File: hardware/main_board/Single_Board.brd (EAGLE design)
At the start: 49.9 x 49.6 mm, 38 parts, among them J1 5520425-3, J2 U.FL, J3 AVR_SPI_PROG_3X2NS, Q1 200mA/40V, Q2 220mA/50V/3.5Ω, U2 MCP1703T-3302E/CB, U3 W25X40CLSNIG, U5 ATMEGA328PB-AU, X2 B2B-PH-K-S, X3 B2B-XH-2, Y1 8MHz

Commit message: More PCB work
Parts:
- moved C8 9.30 mm to (22.4, 13.4)
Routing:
- net VCC: track 156.2 -> 153.4 mm
- net SCK: track 63.2 -> 61.9 mm
- net MOSI: track 73.8 -> 73.2 mm
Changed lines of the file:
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@@
 <attribute name="VALUE" x="41.032" y="7.73" size="0.6096" layer="27" font="vector" ratio="20" rot="R90"/>
 </element>
-<element name="C8" library="SparkFun-Capacitors" library_urn="urn:adsk.eagle:library:510" package="0805" package3d_urn="urn:adsk.eagle:package:37429/1" value="1.0uF" x="25.4" y="4.6" smashed="yes" rot="MR270">
-<attribute name="NAME" x="24.511" y="4.6" size="0.6096" layer="26" font="vector" ratio="20" rot="MR270" align="bottom-center"/>
-<attribute name="PROD_ID" value="CAP-08064" x="51.4" y="52.6" size="1.778" layer="28" rot="MR270" display="off"/>
-<attribute name="VALUE" x="26.289" y="4.6" size="0.6096" layer="28" font="vector" ratio="20" rot="MR270" align="top-center"/>
+<element name="C8" library="SparkFun-Capacitors" library_urn="urn:adsk.eagle:library:510" package="0805" package3d_urn="urn:adsk.eagle:package:37429/1" value="1.0uF" x="22.4" y="13.4" smashed="yes" rot="MR270">
+<attribute name="NAME" x="21.511" y="13.4" size="0.6096" layer="26" font="vector" ratio="20" rot="MR270" align="bottom-center"/>
+<attribute name="PROD_ID" value="CAP-08064" x="48.4" y="61.4" size="1.778" layer="28" rot="MR270" display="off"/>
+<attribute name="VALUE" x="23.289" y="13.4" size="0.6096" layer="28" font="vector" ratio="20" rot="MR270" align="top-center"/>
 </element>
 <element name="Y1" library="SparkFun-Clocks" library_urn="urn:adsk.eagle:library:511" package="RESONATOR-SMD-3.2X1.3" package3d_urn="urn:adsk.eagle:package:37551/1" value="8MHz" x="22" y="17.4" smashed="yes" rot="MR90">
@@
 <attribute name="MANUFACTURER_PART_NUMBER" value="W25X40CLSNIG" x="63.4" y="28" size="1.778" layer="28" rot="MR270" display="off"/>
 <attribute name="NAME" x="21.035" y="9.2766" size="1.27" layer="26" ratio="6" rot="SMR270"/>
-<attribute name="VALUE" x="21.035" y="7.7272" size="1.27" layer="22" ratio="6" rot="SMR270"/>
 <attribute name="VENDOR" value="Winbond" x="63.4" y="28" size="1.778" layer="28" rot="MR270" display="off"/>
 </element>
@@
 <wire x1="34.27" y1="26.96" x2="34.27" y2="24.47" width="0.1524" layer="1"/>
 <wire x1="34.27" y1="24.47" x2="34.26" y2="24.46" width="0.1524" layer="1"/>
-<wire x1="34.27" y1="26.96" x2="34.04" y2="26.96" width="0.1524" layer="1"/>
 <wire x1="36.29" y1="26.56" x2="34.27" y2="27.42" width="0.1524" layer="1"/>
 <wire x1="34.27" y1="27.42" x2="34.27" y2="26.96" width="0.1524" layer="1"/>
@@
 <wire x1="21.035" y1="6.6" x2="21.035" y2="8.4638" width="0.1524" layer="16"/>
 <wire x1="19.765" y1="4.965" x2="21.035" y2="6.235" width="0.1524" layer="16"/>
-<wire x1="25.4" y1="5.5" x2="24.5" y2="5.5" width="0.1524" layer="16"/>
-<wire x1="23.4" y1="6.6" x2="21.035" y2="6.6" width="0.1524" layer="16"/>
-<wire x1="24.5" y1="5.5" x2="23.4" y2="6.6" width="0.1524" layer="16"/>
-<wire x1="21.035" y1="6.6" x2="16.2" y2="6.6" width="0.1524" layer="16"/>
+<wire x1="16.2" y1="6.6" x2="21.035" y2="6.6" width="0.1524" layer="16"/>
 <wire x1="16.2" y1="6.6" x2="13.6" y2="9.2" width="0.1524" layer="16"/>
 <wire x1="13.6" y1="9.2" x2="13.6" y2="11.2" width="0.1524" layer="16"/>
@@
 <wire x1="32.2" y1="16" x2="30.8" y2="14.6" width="0.1524" layer="16"/>
 <wire x1="30.8" y1="14.6" x2="26.2" y2="14.6" width="0.1524" layer="16"/>
-<wire x1="16" y1="11.3" x2="17.3" y2="10" width="0.1524" layer="16"/>
-<wire x1="17.3" y1="10" x2="17.4" y2="10" width="0.1524" layer="16"/>
-<via x="17.4" y="10" extent="1-16" drill="0.35"/>
-<wire x1="17.4" y1="10" x2="19.4" y2="10" width="0.1524" layer="1"/>
-<wire x1="19.4" y1="10" x2="23" y2="13.6" width="0.1524" layer="1"/>
-<via x="23" y="13.6" extent="1-16" drill="0.35"/>
-<wire x1="23" y1="13.6" x2="24.82" y2="13.6" width="0.1524" layer="16"/>
+<via x="23.4" y="8.2" extent="1-16" drill="0.35"/>
+<wire x1="23.4" y1="8.2" x2="23.4" y2="9.8" width="0.1524" layer="1"/>
+<wire x1="23.4" y1="9.8" x2="26.6" y2="13" width="0.1524" layer="1"/>
+<via x="26.6" y="13" extent="1-16" drill="0.35"/>
+<wire x1="26.2" y1="13.6" x2="26.2" y2="13.4" width="0.1524" layer="16"/>
+<wire x1="26.2" y1="13.4" x2="26.6" y2="13" width="0.1524" layer="16"/>
+<wire x1="22.4" y1="14.3" x2="23.1" y2="13.6" width="0.1524" layer="16"/>
+<wire x1="23.1" y1="13.6" x2="24.82" y2="13.6" width="0.1524" layer="16"/>
+<wire x1="21.035" y1="6.6" x2="22.6" y2="6.6" width="0.1524" layer="16"/>
+<wire x1="23.4" y1="7.4" x2="23.4" y2="8.2" width="0.1524" layer="16"/>
+<wire x1="22.6" y1="6.6" x2="23.4" y2="7.4" width="0.1524" layer="16"/>
 </signal>
 <signal name="GND">
@@
 </polygon>
 <via x="31.6" y="22.2" extent="1-16" drill="0.35"/>
-<via x="21.8" y="14.4" extent="1-16" drill="0.35"/>
+<via x="20.8" y="12.8" extent="1-16" drill="0.35"/>
 </signal>
 <signal name="SDA">
@@
 <wire x1="31.595" y1="25.325" x2="28.2" y2="25.325" width="0.1524" layer="1"/>
 <contactref element="U5" pad="27"/>
-<wire x1="30.2" y1="9.82" x2="30.4" y2="10.02" width="0.1524" layer="16"/>
 <via x="30.4" y="12.4" extent="1-16" drill="0.35"/>
 <wire x1="30.4" y1="12.4" x2="30.2" y2="12.6" width="0.1524" layer="1"/>
@@
 <contactref element="R6" pad="2"/>
 <wire x1="26.2" y1="9.82" x2="26.18" y2="9.8" width="0.1524" layer="16"/>
-<wire x1="22.2" y1="11.6" x2="20" y2="11.6" width="0.1524" layer="16"/>
+<wire x1="22.2" y1="11.4" x2="20.2" y2="11.4" width="0.1524" layer="16"/>
+<wire x1="20.2" y1="11.4" x2="20" y2="11.6" width="0.1524" layer="16"/>
 <via x="20" y="11.6" extent="1-16" drill="0.35"/>
 <wire x1="20" y1="11.6" x2="18" y2="11.6" width="0.1524" layer="1"/>
@@
 <wire x1="13.8" y1="12.8" x2="13.35" y2="13.25" width="0.1524" layer="16"/>
 <wire x1="13.35" y1="13.25" x2="13.35" y2="14.2" width="0.1524" layer="16"/>
-<wire x1="26.18" y1="9.8" x2="24" y2="9.8" width="0.1524" layer="16"/>
-<wire x1="24" y1="9.8" x2="22.2" y2="11.6" width="0.1524" layer="16"/>
+<wire x1="26.18" y1="9.8" x2="23.8" y2="9.8" width="0.1524" layer="16"/>
+<wire x1="23.8" y1="9.8" x2="22.2" y2="11.4" width="0.1524" layer="16"/>
 <wire x1="12.3" y1="11.4" x2="13.7" y2="12.8" width="0.1524" layer="16"/>
 <wire x1="13.7" y1="12.8" x2="13.8" y2="12.8" width="0.1524" layer="16"/>
@@
 <wire x1="21.422225" y1="22" x2="20.840825" y2="22.5814" width="0.1524" layer="1"/>
 <wire x1="16.2" y1="16.2" x2="16.2" y2="3.6" width="0.1524" layer="1"/>
-<wire x1="22.305" y1="1.6" x2="22.305" y2="3.5362" width="0.1524" layer="16"/>
-<wire x1="16.2" y1="3.6" x2="18.2" y2="1.6" width="0.1524" layer="16"/>
-<wire x1="18.2" y1="1.6" x2="22.305" y2="1.6" width="0.1524" layer="16"/>
+<wire x1="22.305" y1="2" x2="22.305" y2="3.5362" width="0.1524" layer="16"/>
+<wire x1="16.2" y1="3.6" x2="17.8" y2="2" width="0.1524" layer="16"/>
+<wire x1="17.8" y1="2" x2="22.305" y2="2" width="0.1524" layer="16"/>
 <wire x1="42.73" y1="23" x2="38.73" y2="27" width="0.1524" layer="16"/>
 <wire x1="38.73" y1="27" x2="22.8" y2="27" width="0.1524" layer="16"/>
@@
 <contactref element="U5" pad="17"/>
 <contactref element="J3" pad="3"/>
-<wire x1="20.5" y1="23.1" x2="20.5" y2="24.4" width="0.1524" layer="16"/>
 <via x="20.6" y="22" extent="1-16" drill="0.35"/>
 <wire x1="20.6" y1="22" x2="20.5" y2="22.1" width="0.1524" layer="16"/>
@@
 <wire x1="25.4" y1="46" x2="25.375" y2="46" width="0.1524" layer="1"/>
 <wire x1="20.5" y1="41.5" x2="21.8" y2="42.8" width="0.1524" layer="16"/>
-<wire x1="22.625" y1="46" x2="22.625" y2="48.625" width="0.1524" layer="1"/>
-<wire x1="22.625" y1="48.625" x2="23" y2="49" width="0.1524" layer="1"/>
-<wire x1="23" y1="49" x2="25.2" y2="49" width="0.1524" layer="1"/>
-<wire x1="25.2" y1="49" x2="25.6" y2="48.6" width="0.1524" layer="1"/>
+<wire x1="22.625" y1="46" x2="22.625" y2="48.6" width="0.1524" layer="1"/>
+<wire x1="22.625" y1="48.6" x2="25.6" y2="48.6" width="0.1524" layer="1"/>
 <wire x1="25.6" y1="48.6" x2="25.6" y2="46.2" width="0.1524" layer="1"/>
 <wire x1="25.6" y1="46.2" x2="25.4" y2="46" width="0.1524" layer="1"/>
@@
 <contactref element="U5" pad="20"/>
 <contactref element="C3" pad="2"/>
-<wire x1="33.18" y1="14.4" x2="33.33" y2="14.55" width="0.1524" layer="16"/>
 <wire x1="36.15" y1="14.4" x2="36.6" y2="14.85" width="0.1524" layer="16"/>
 <wire x1="33.18" y1="14.4" x2="36.15" y2="14.4" width="0.1524" layer="16"/>

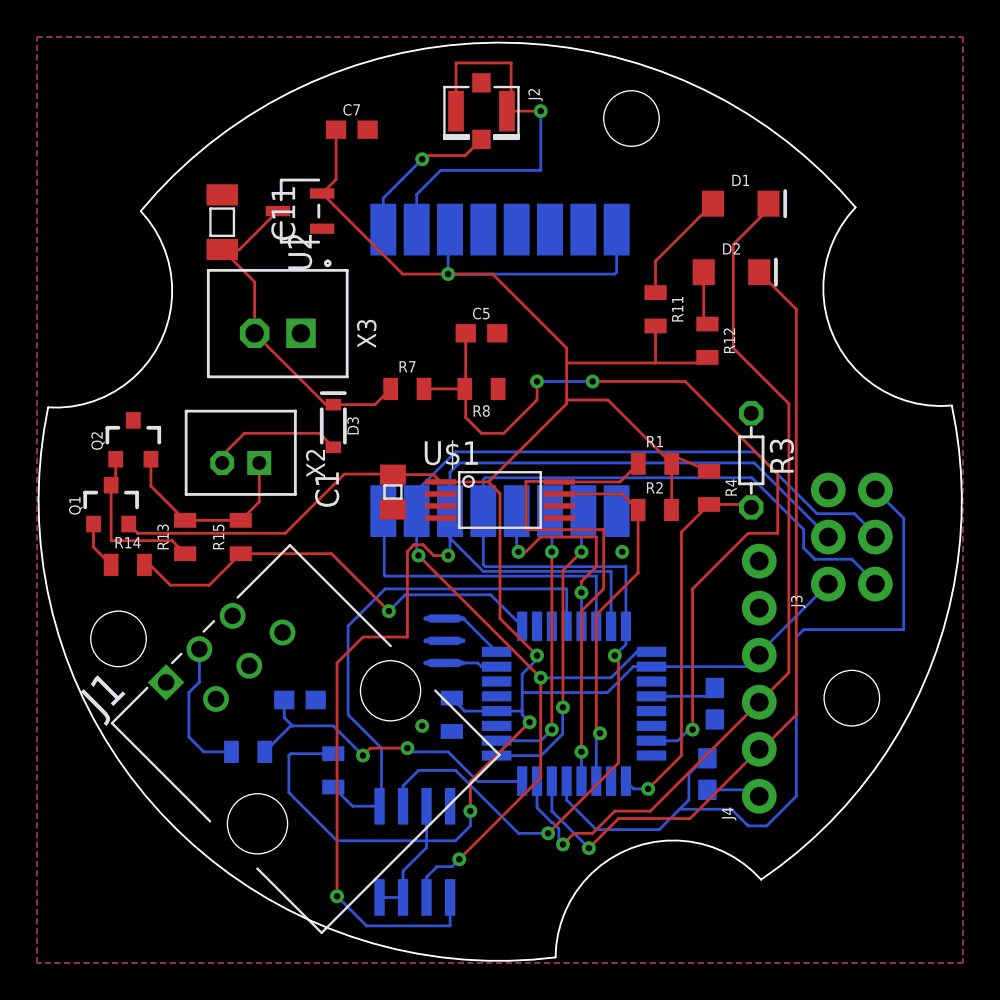
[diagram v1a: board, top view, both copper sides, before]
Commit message: Hardware work. Added elevation to station meta data
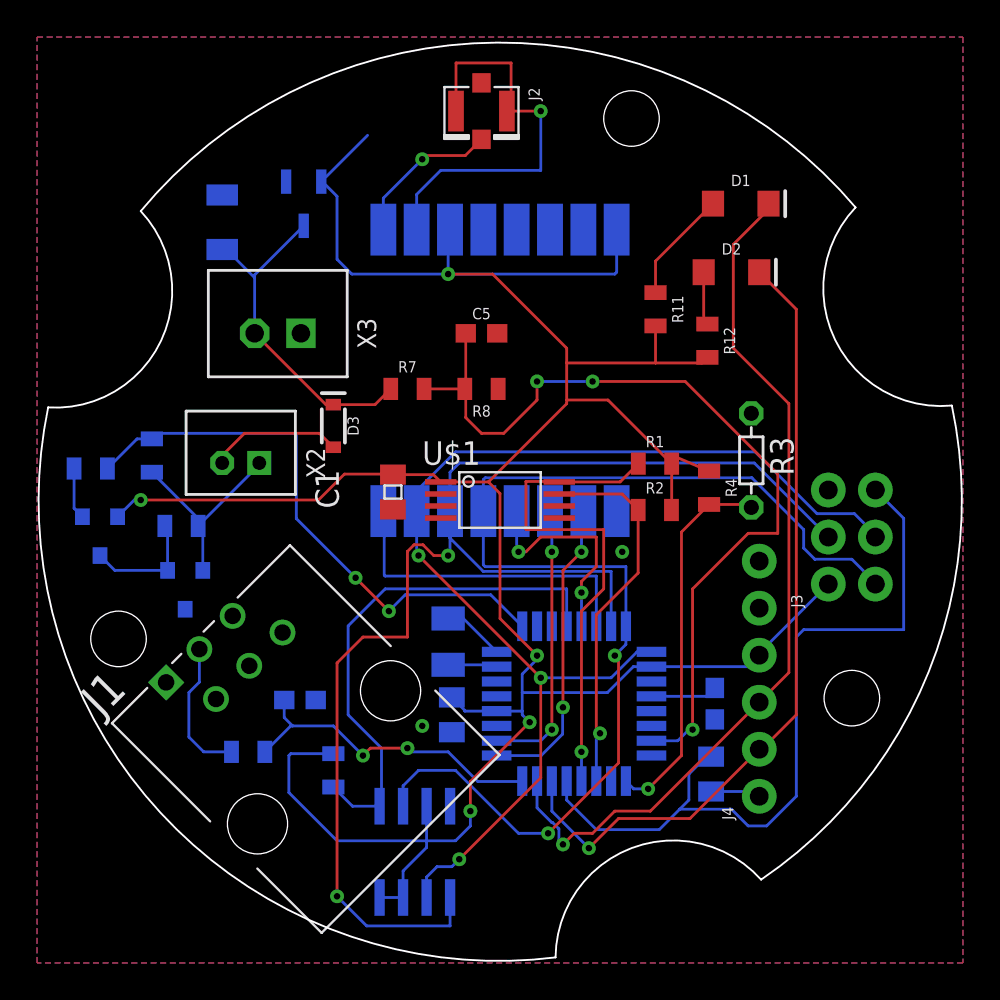
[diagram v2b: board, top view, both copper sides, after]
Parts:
- removed C7: 1.0uF, SparkFun-Capacitors:0603
- removed C8: 1.0uF, SparkFun-Capacitors:0805
- removed Y1: 8MHz, SparkFun-Clocks:RESONATOR-SMD-3.2X1.3
- added C6: 1uF, capsmd:0805
- added X1: 32.768KHZ-FC-135, main_board:32.768KHZ-FC-135
- C4: device SparkFun-Capacitors:0603 -> main_board:0805
- R11, R12: value (none) -> 1k
- moved Q2 8.48 mm to (8.00, 20.2), flipped to the bottom, turned to 180 degrees
- moved R15 6.51 mm to (6.20, 27.4), flipped to the bottom, turned to 270 degrees
- moved R14 5.57 mm to (2.90, 26.7), flipped to the bottom, turned to 180 degrees
- moved Q1 1.71 mm to (3.40, 23.1), flipped to the bottom, turned to 180 degrees
- moved R13 0.63 mm to (7.80, 23.6), flipped to the bottom, turned to 180 degrees
- moved U2 0.45 mm to (14.4, 41.0), flipped to the bottom, turned to 180 degrees
- moved C4 0.20 mm to (36.4, 10.2), turned to 90 degrees
- flipped C11 to the bottom
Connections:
- net AT_RST: now also C4.2; no longer C4.1
- net GND: now also C6.1; no longer C7.2, C8.2, Y1.2
- net N$11: now also C4.1; no longer C4.2
- net N$7: now also X1.2; no longer Y1.1
- net N$8: now also X1.1; no longer Y1.3
- net VCC: now also C6.2; no longer C7.1, C8.1
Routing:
- net PWM_SOLAR: track 23.9 -> 30.9 mm, vias 1 -> 2
- net N$12: track 8.79 -> 6.44 mm
- net VCC: track 153.4 -> 155.5 mm, vias 4 -> 5
- net N$9: track 10.6 -> 11.2 mm

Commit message: Reworked board to put more components on bottom side (=less soldering)
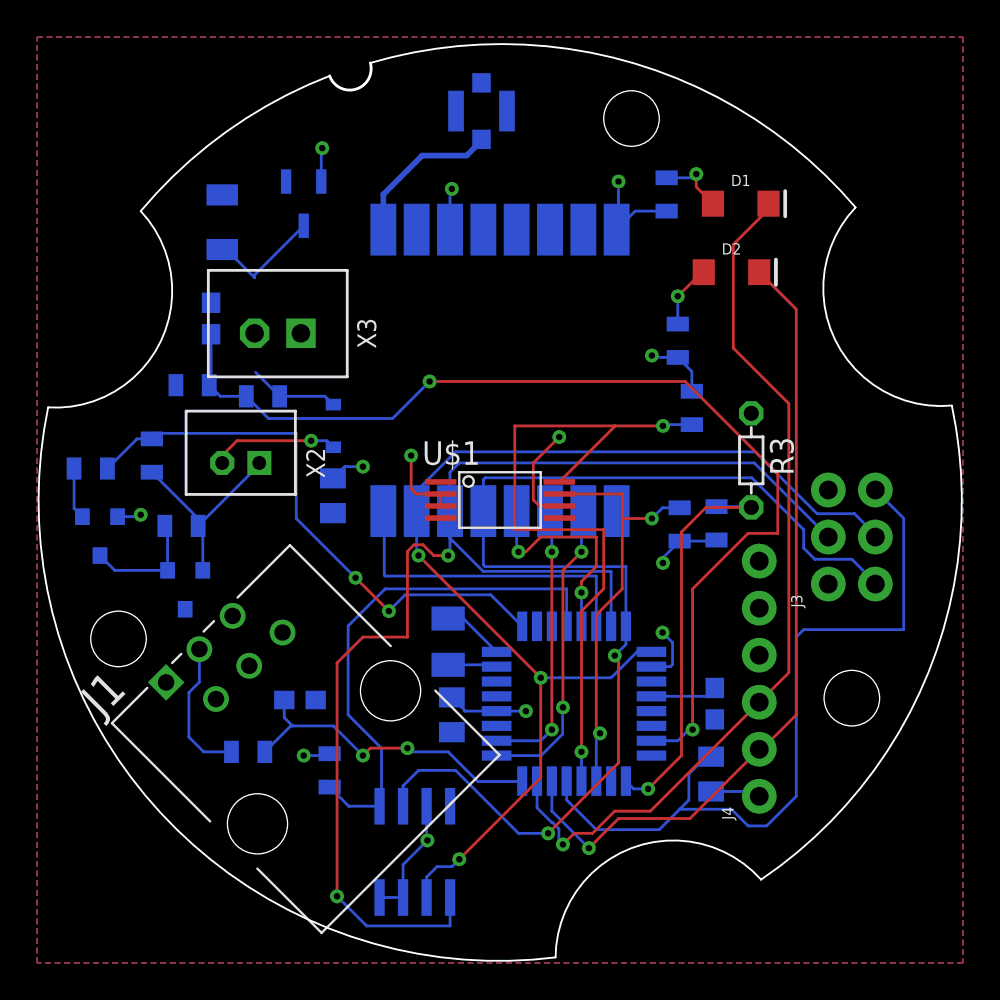
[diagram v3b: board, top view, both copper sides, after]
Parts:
- moved R8 15.6 mm to (8.40, 31.2), flipped to the bottom
- moved C5 14.6 mm to (9.40, 34.8), flipped to the bottom, turned to 90 degrees
- moved R7 7.81 mm to (12.2, 30.6), flipped to the bottom
- moved R11 6.23 mm to (34.0, 41.5), flipped to the bottom
- moved R1 3.61 mm to (35.4, 30.0), flipped to the bottom, turned to 90 degrees
- moved C1 3.25 mm to (16.0, 25.2), flipped to the bottom
- moved R4 1.96 mm to (36.7, 23.7), flipped to the bottom, turned to 90 degrees
- moved R12 1.60 mm to (34.6, 33.6), flipped to the bottom
- moved R2 1.55 mm to (34.7, 23.7), flipped to the bottom, turned to 270 degrees
- moved R9 0.20 mm to (15.8, 10.4)
- flipped D3 to the bottom
- flipped J2 to the bottom
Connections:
- removed net RF_GND: J2.1, J2.2, U$2.GND@1
- net GND: now also J2.1, J2.2, U$2.GND@1
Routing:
- net VCC: track 155.5 -> 36.4 mm, vias 5 -> 11
- net RF_GND: track 22.4 -> 0.00 mm, vias 1 -> 0
- net SCL: track 27.4 -> 38.3 mm, vias 1 -> 2
- net GND: track 0.00 -> 9.68 mm
- net BATT_SENSE: track 47.0 -> 56.3 mm, vias 3 -> 2
- net VIN: track 18.6 -> 11.3 mm
- net SDA: track 20.4 -> 23.0 mm, vias 1 -> 2
- net N$4: track 6.08 -> 3.66 mm, vias 0 -> 1
- net TEMP_SENSE: track 20.4 -> 22.2 mm
- net N$6: track 2.88 -> 3.44 mm, vias 0 -> 1
- net VSOLAR: track 7.21 -> 6.88 mm, vias 0 -> 1
- net ANT: track 8.32 -> 8.48 mm, vias 1 -> 0
- added copper zone on layer 1, net VCC
- removed copper zone on layer 1, net GND
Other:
- board size 49.9 x 49.6 mm -> 49.9 x 49.5 mm

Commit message: Added daylight indicators
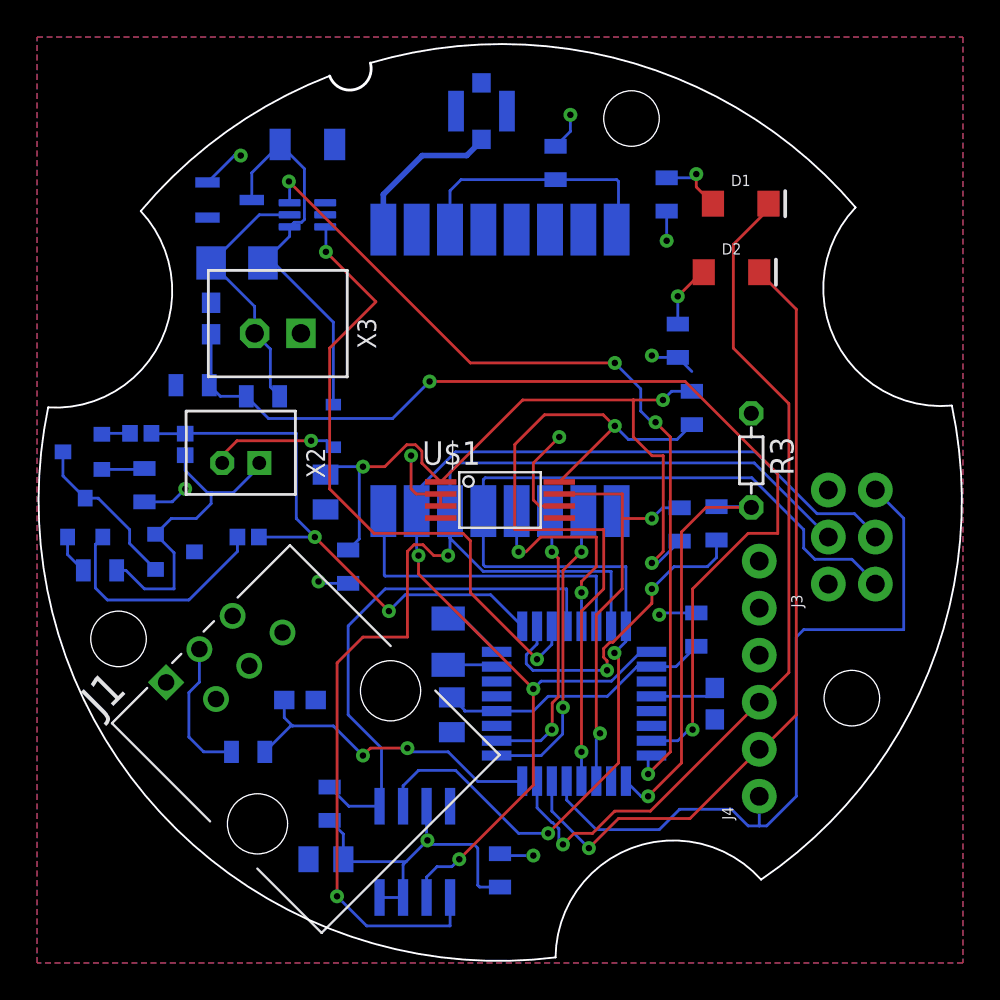
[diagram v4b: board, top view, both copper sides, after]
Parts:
- removed C4: 100nF, main_board:0805
- removed R15: 10k, SparkFun-Resistors:0805
- added C7: 1uF, capsmd:0805
- added Q3: 500mA/300V, SparkFun-DiscreteSemi:SOT23-3
- added R10, R16, R17, R18, R5: 0, SparkFun-Resistors:0805
- added R19, R20: 500k, SparkFun-Resistors:0402
- added R21: 0.1, SparkFun-Resistors:1206
- added U1: INA199A3DCKR, main_board:SOT65P210X110-6N
- R13: value 33k -> 0
- R14: value 33k -> 20k; device SparkFun-Resistors:0805 -> SparkFun-Resistors:0402
- moved C11 6.23 mm to (14.6, 44.2), turned to 0 degrees
- moved R14 5.26 mm to (8.00, 28.0), turned to 90 degrees
- moved R13 5.01 mm to (3.40, 21.2)
- moved Q1 4.59 mm to (2.50, 27.6), turned to 270 degrees
- moved U2 4.00 mm to (10.4, 41.2), turned to 90 degrees
- moved Q2 2.09 mm to (7.40, 22.2), turned to 90 degrees
- moved R9 1.80 mm to (15.8, 8.60), turned to 90 degrees
- moved C1 0.45 mm to (15.6, 25.4)
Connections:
- new net CUR_SENSE: U1.6, U5.24
- new net CUR_SENSE_PWR: U1.3, U5.11
- new net FLASH_VCC: C7.2, R16.1, R9.1, U3.3, U3.7, U3.8
- new net MAG_VCC: C1.2, R1.2, R17.1, R2.2, U$1.VCC
- new net MCU_VCC: C6.2, R5.1, U5.18, U5.4
- new net N$1: R10.1, U$2.SW, U$2.VCC
- new net N$10: Q3.1, R20.1
- new net N$3: Q1.2, R18.1
- new net N$5: Q3.2, R13.1
- new net TEMP_PWR: R4.1, U5.10
- net AT_RST: now also J4.1; no longer C4.2
- net GND: now also C7.1, U1.1, U1.2
- net N$11: now also R21.1, R7.1, U1.5, X3.2; no longer C4.1, J4.1
- net N$12: now also Q3.3; no longer R13.1
- net N$13: now also R19.1; no longer R14.1
- net N$9: now also R14.1; no longer R15.2
- net PWM_SOLAR: now also R19.2, R20.2; no longer R15.1
- net VCC: now also R10.2, R16.2, R17.2, R18.2, R5.2; no longer C1.2, C6.2, Q1.2, R1.2, R2.2, R4.1, R9.1, U$1.VCC, U$2.SW, U$2.VCC, U3.3, U3.7, U3.8, U5.18, U5.4
- net VIN: now also R21.2, U1.4; no longer R7.1, X3.2
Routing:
- net CUR_SENSE: track 0.00 -> 48.0 mm, vias 0 -> 4
- net MAG_VCC: track 0.00 -> 40.5 mm, vias 0 -> 3
- net CUR_SENSE_PWR: track 0.00 -> 35.1 mm, vias 0 -> 2
- net VCC: track 36.4 -> 17.0 mm, vias 11 -> 8
- net FLASH_VCC: track 0.00 -> 18.7 mm, vias 0 -> 1
- net TEMP_PWR: track 0.00 -> 17.6 mm, vias 0 -> 2
- net MCU_VCC: track 0.00 -> 15.0 mm
- net N$1: track 0.00 -> 14.1 mm
- net N$10: track 0.00 -> 12.7 mm
- net N$11: track 2.71 -> 14.0 mm
- net VIN: track 11.3 -> 21.3 mm
- net N$9: track 11.2 -> 17.3 mm
- net N$12: track 6.44 -> 8.83 mm
- net N$3: track 0.00 -> 2.32 mm
- net N$5: track 0.00 -> 2.15 mm
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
